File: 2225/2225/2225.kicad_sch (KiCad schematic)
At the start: 4 parts

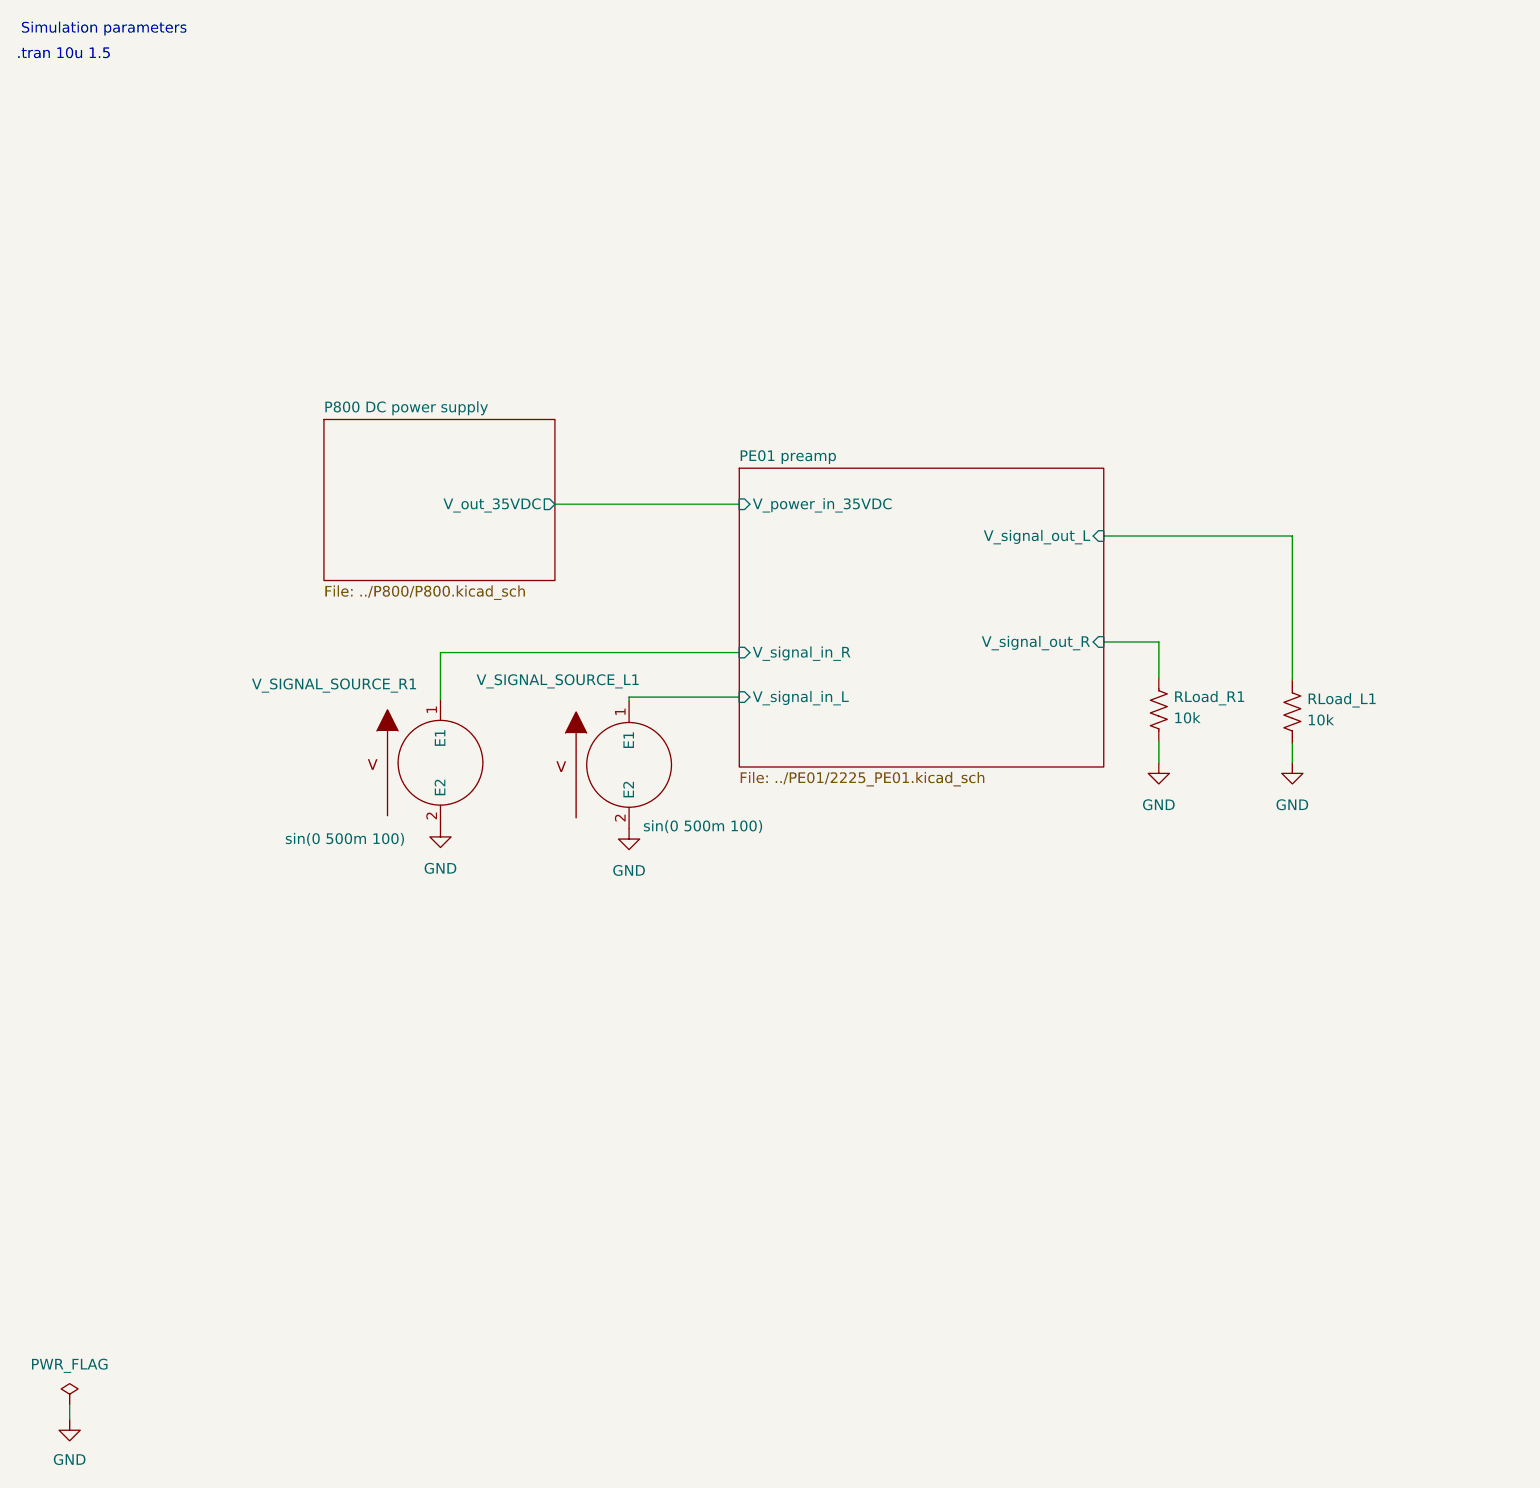
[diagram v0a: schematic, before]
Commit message: Connected transformer to P800 in 2225.kicad_sch; changed transformer model resistances in 2225.lib
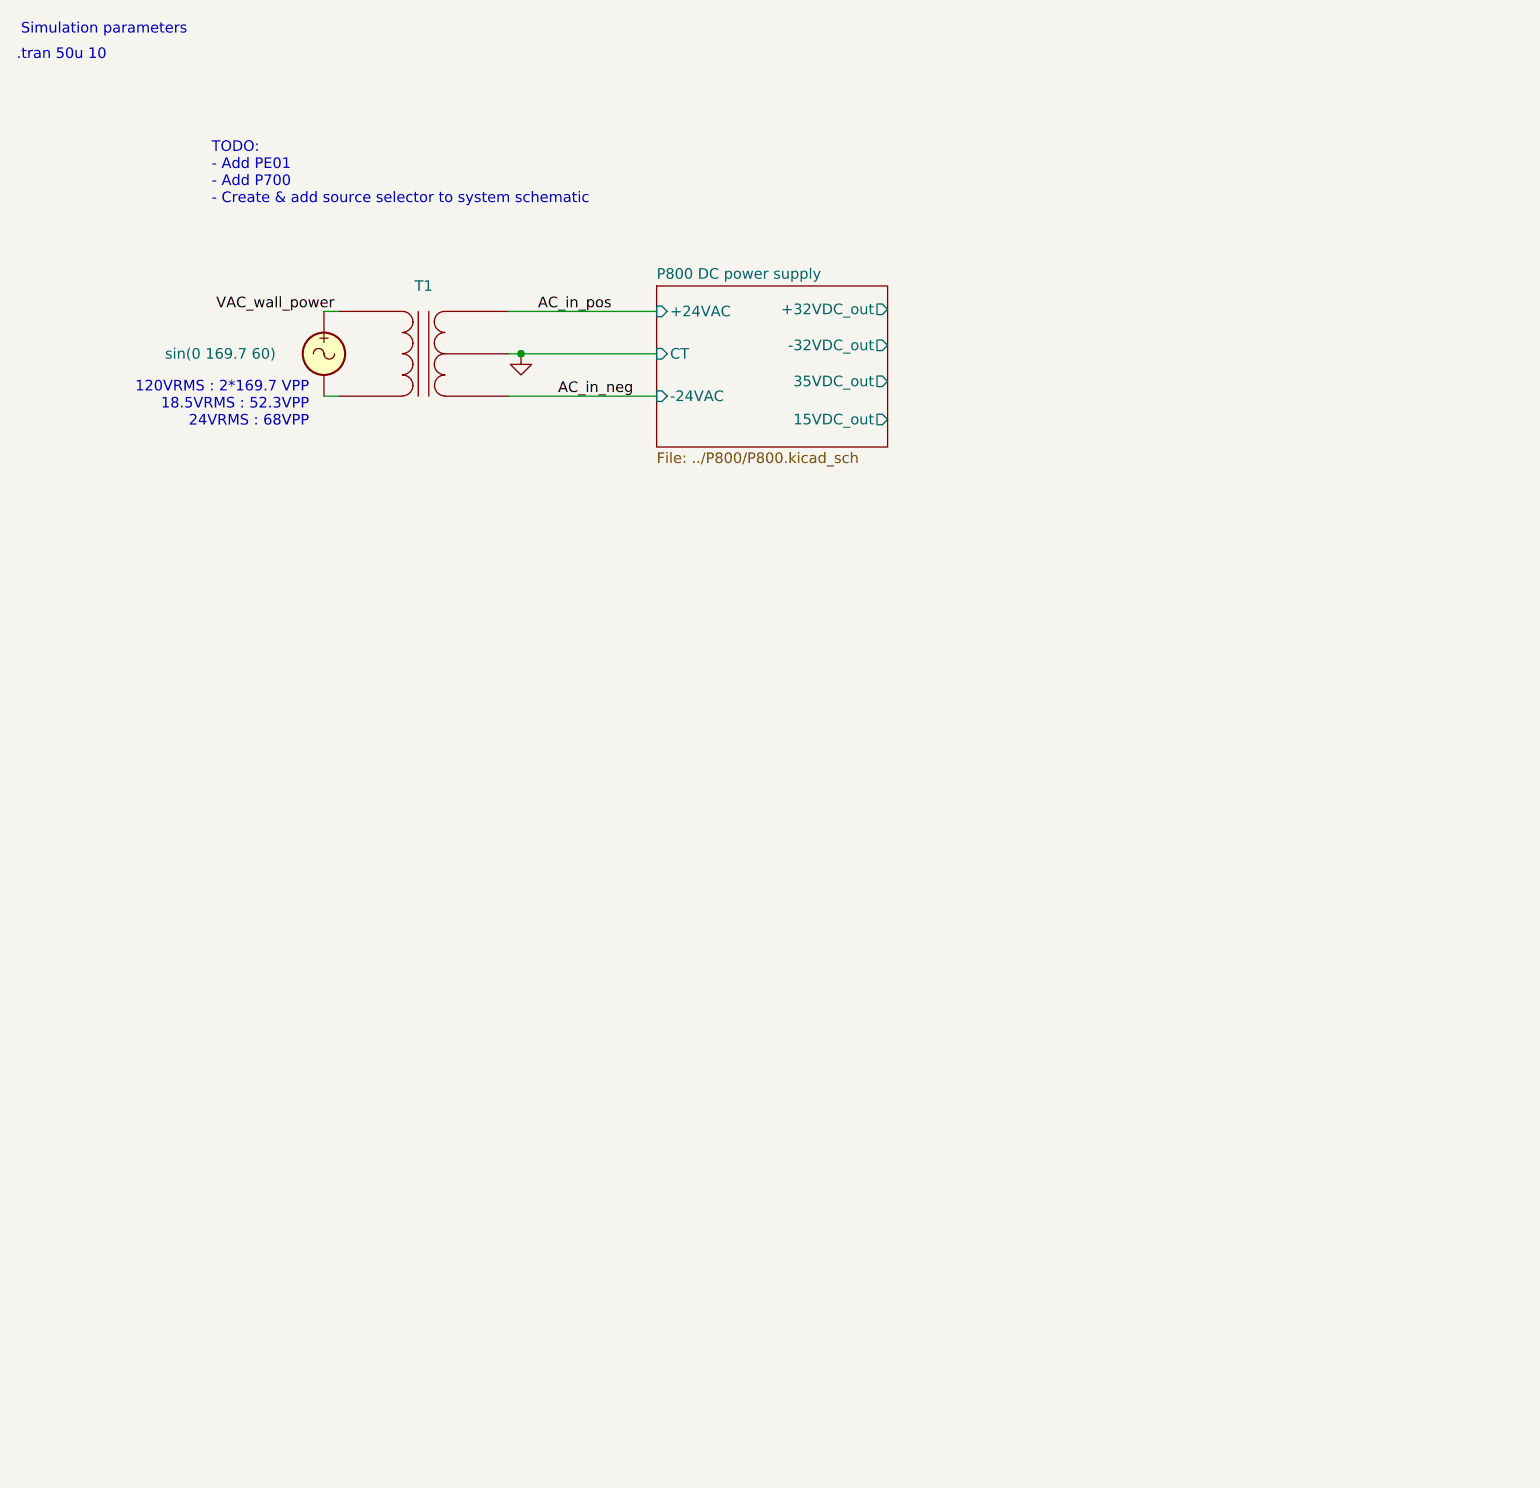
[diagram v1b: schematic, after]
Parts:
- removed RLoad_L1, RLoad_R1: 10k, Resistor_THT:R_Axial_DIN0309_L9.0mm_D3.2mm_P12.70mm_Horizontal, symbol Device:R_US
- removed V_SIGNAL_SOURCE_L1, V_SIGNAL_SOURCE_R1: 0, symbol pspice:VSOURCE
- added T1: Transformer_1P_SS, symbol Device:Transformer_1P_SS
- added VAC_1: VSIN, symbol Simulation_SPICE:VSIN
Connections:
- net GND: now also T1.4 (SC)
- new net: T1.2 (AB), VAC_1.2
- new net AC_in_neg: T1.3 (SA)
- new net AC_in_pos: T1.5 (SB)
- new net VAC_wall_power: T1.1 (AA), VAC_1.1
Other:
- removed sheet PE01 preamp
- sheet P800 DC power supply ports: added +24VAC, +32VDC_out, -24VAC, -32VDC_out, 15VDC_out, 35VDC_out, CT; removed V_out_35VDC
- note added: ".tran 50u 10"
- note added: "120VRMS : 2*169.7 VPP 18.5VRMS : 52.3VPP 24VRMS : 68VPP"
- note added: "TODO: - Add PE01 - Add P700 - Create & add source selector to system schematic"
- note removed: ".tran 10u 1.5"

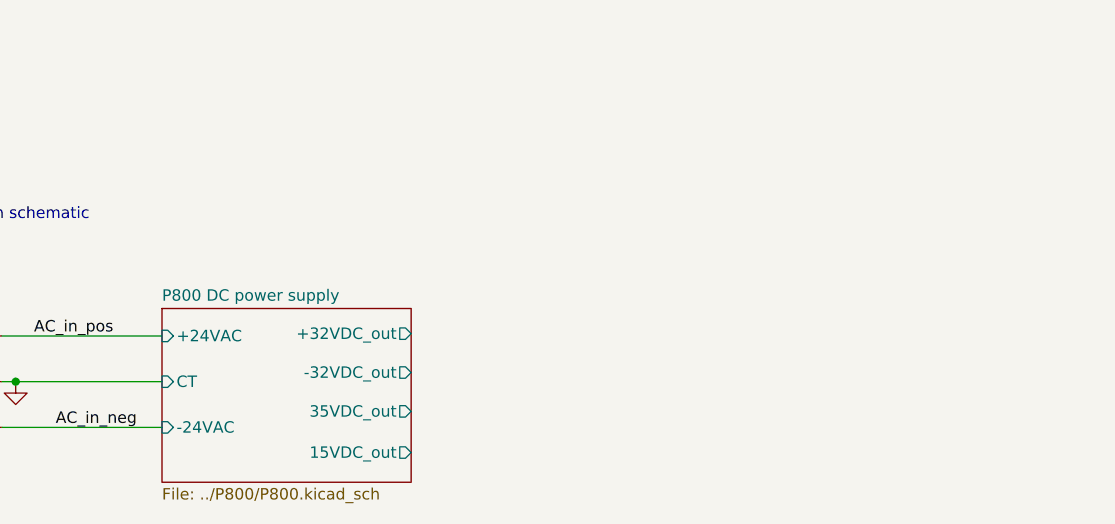
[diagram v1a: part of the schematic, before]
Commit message: Connected P800 (DC supply) to PE01 tone board, audio source to PE01, and PE01 to dummy P700 main amplifier. Changed some hierarchical label names in multiple schematics.
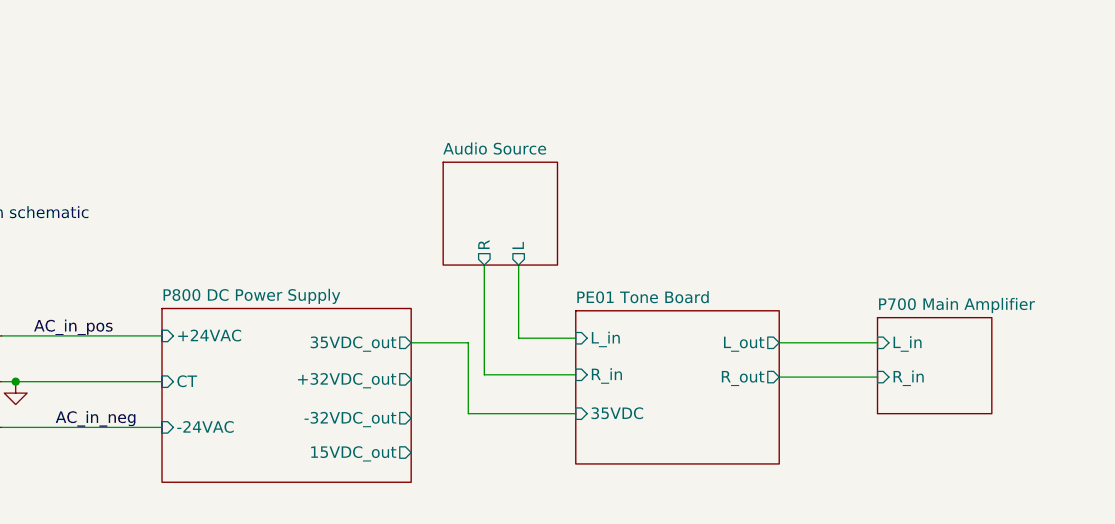
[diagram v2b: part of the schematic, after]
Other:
- sheet P800 DC power supply renamed P800 DC Power Supply
- added sheet Audio Source (audio_source.kicad_sch)
- added sheet P700 Main Amplifier (../P700/P700.kicad_sch)
- added sheet PE01 Tone Board (../PE01/2225_PE01.kicad_sch)

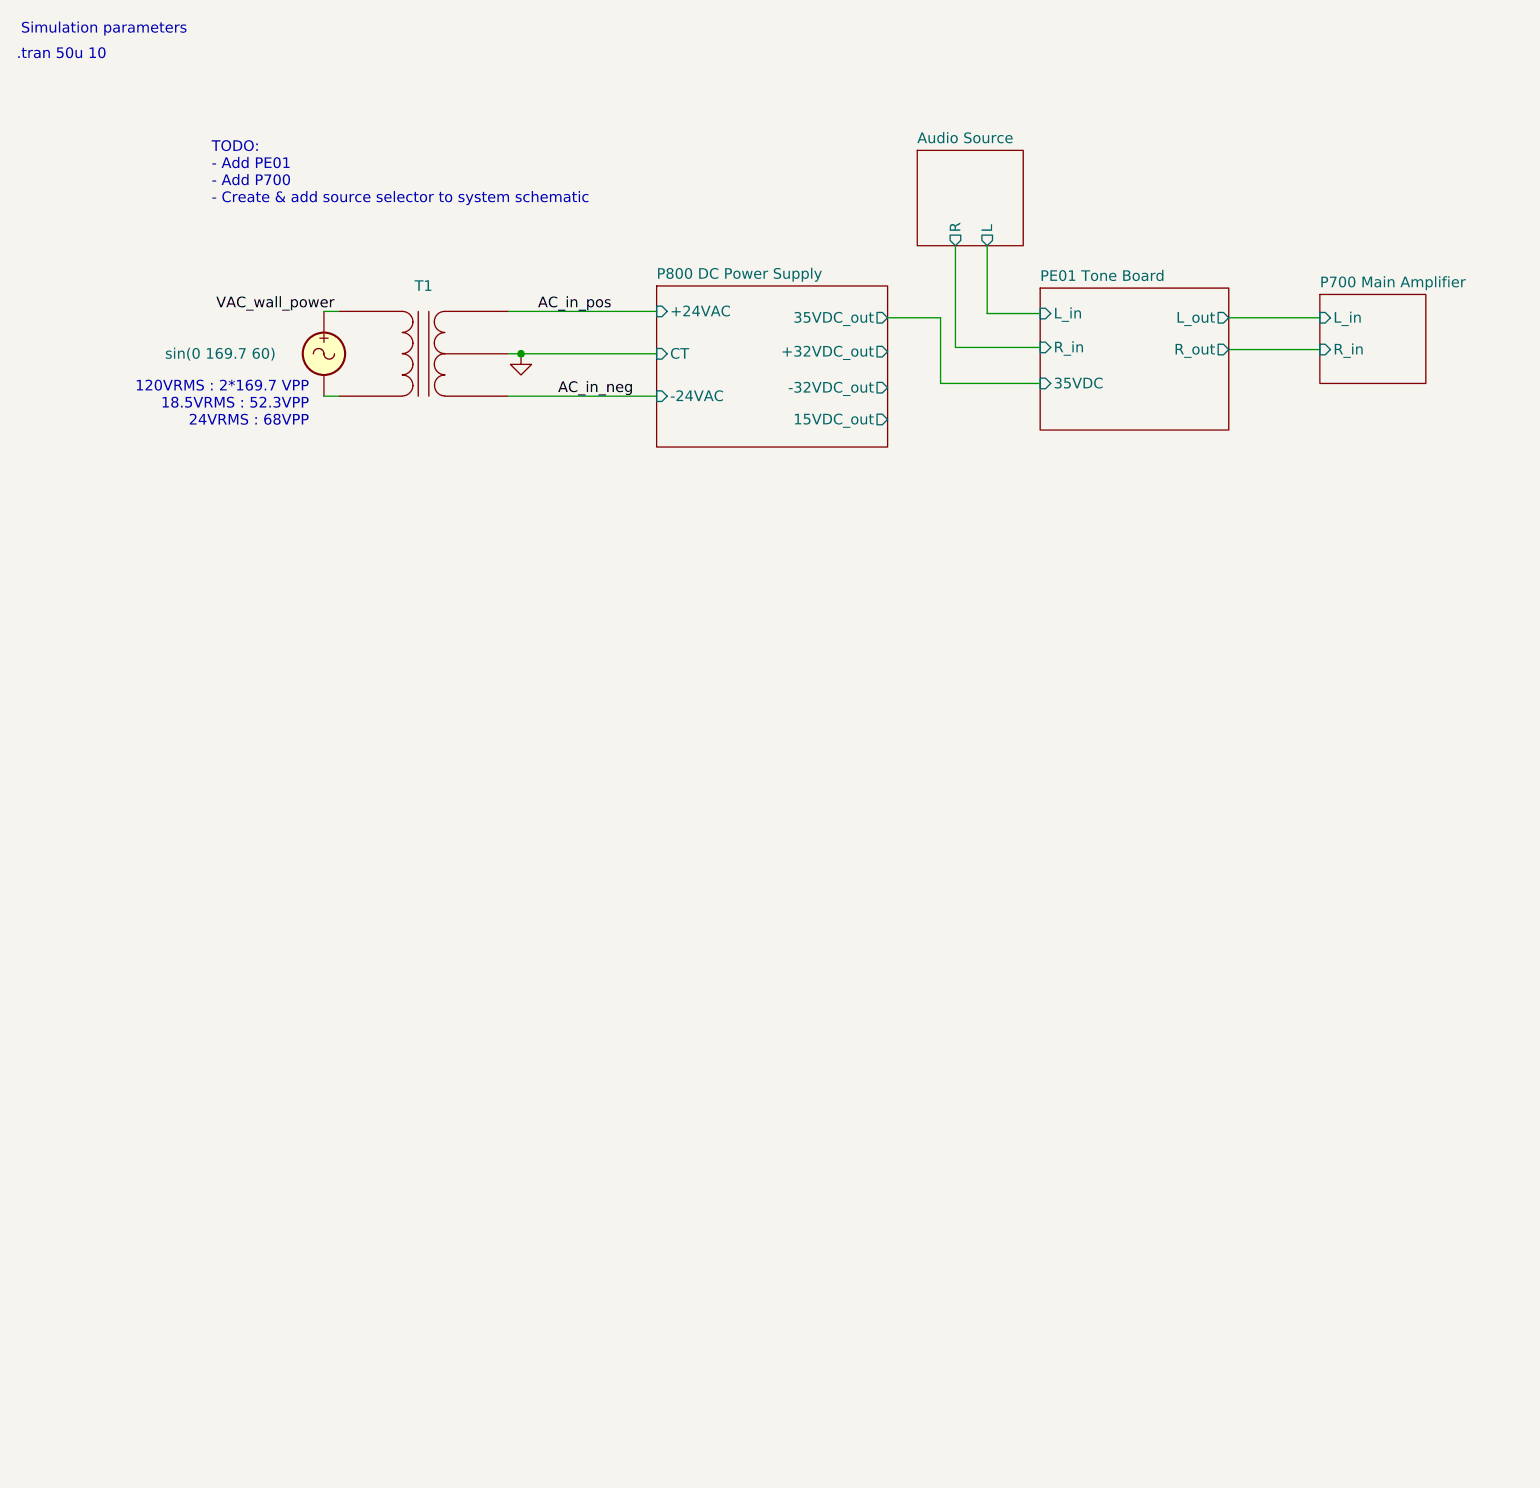
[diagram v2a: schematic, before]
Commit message: Added dummy power inputs to P700 block in 2225.kicad_sch (system block diagram)
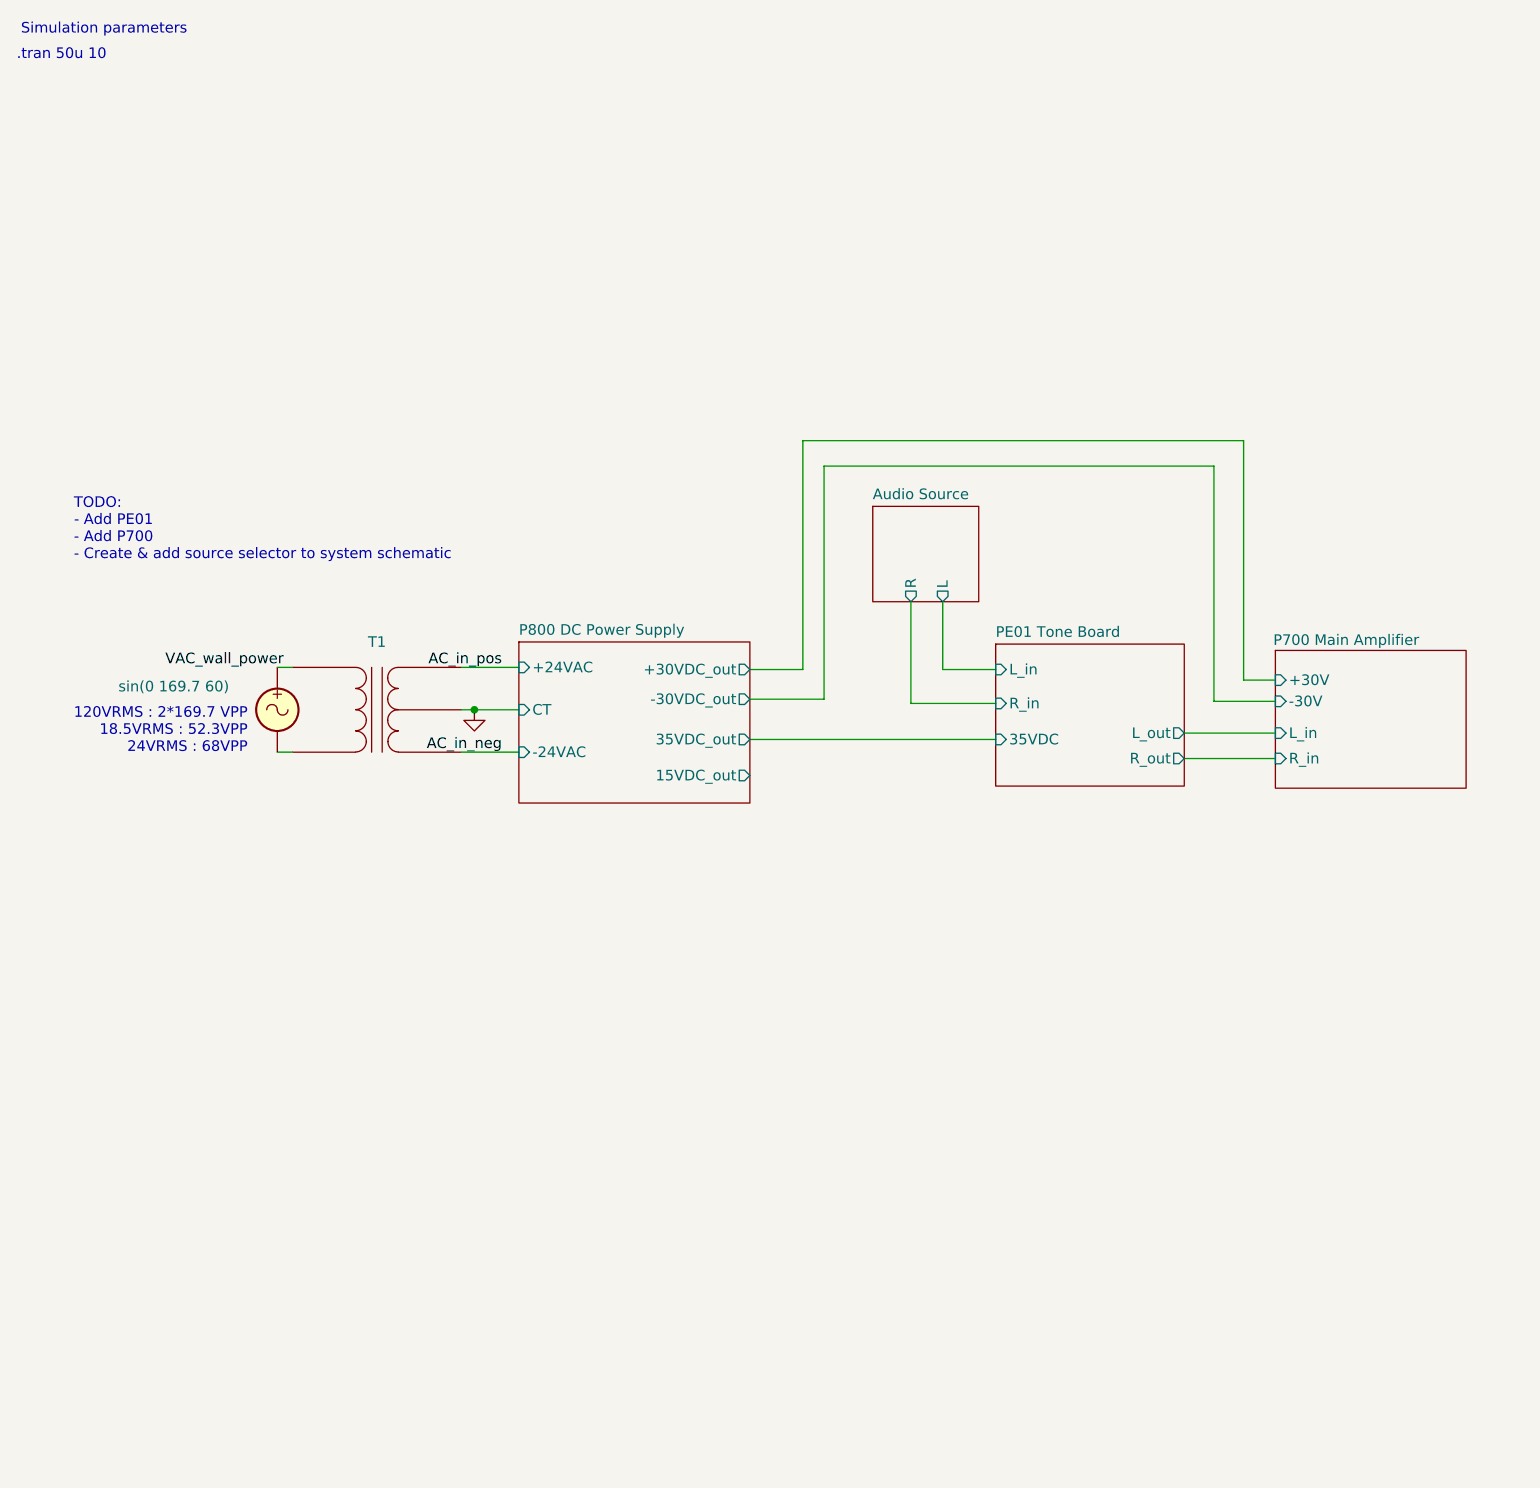
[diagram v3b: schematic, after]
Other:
- sheet P700 Main Amplifier ports: added +30V, -30V; removed none
- sheet P800 DC Power Supply ports: added +30VDC_out, -30VDC_out; removed +32VDC_out, -32VDC_out
- moved on the sheet: T1
